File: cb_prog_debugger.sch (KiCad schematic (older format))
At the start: 49 parts, among them J1 USB_HOST, J2 Conn_01x03_Male, J3 USB_DEBUG, J4 Conn_02x03_Odd_Even, J5 ZIF16, U1 93LC56B, U2 LM1117-3.3, U3 CH341A, U4 FT232H, Y1 12 MHz, Y2 12 MHz

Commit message: Add differential net names
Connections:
- net USBDBG-: now reaches J3.2 (D-), U4.6 (DM)
- net USBDBG+: now reaches J3.3 (D+), U4.7 (DP)
- net USBHOST+: now reaches J1.3 (D+), U3.10 (UD+)
- net USBHOST-: now reaches J1.2 (D-), U3.11 (UD-)
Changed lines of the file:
@@
 Wire Wire Line
 	1400 6700 1400 6650
+Text Label 2600 2900 0    60   ~ 0
+USBHOST+
+Text Label 2600 3000 0    60   ~ 0
+USBHOST-
+Text Label 3800 5550 0    60   ~ 0
+USBDBG+
+Text Label 3800 5650 0    60   ~ 0
+USBDBG-
 $EndSCHEMATC

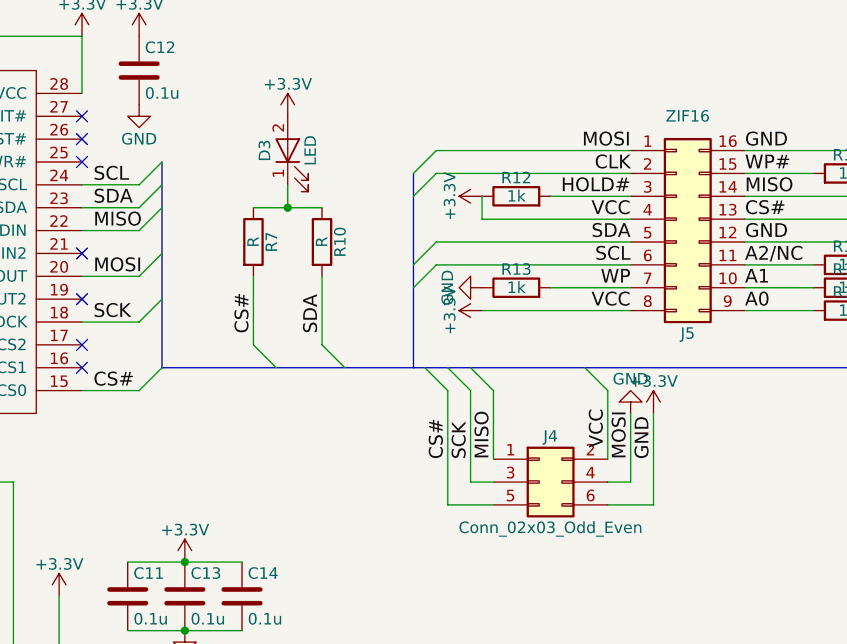
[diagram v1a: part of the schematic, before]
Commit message: Fix shorted 3.3V-GND
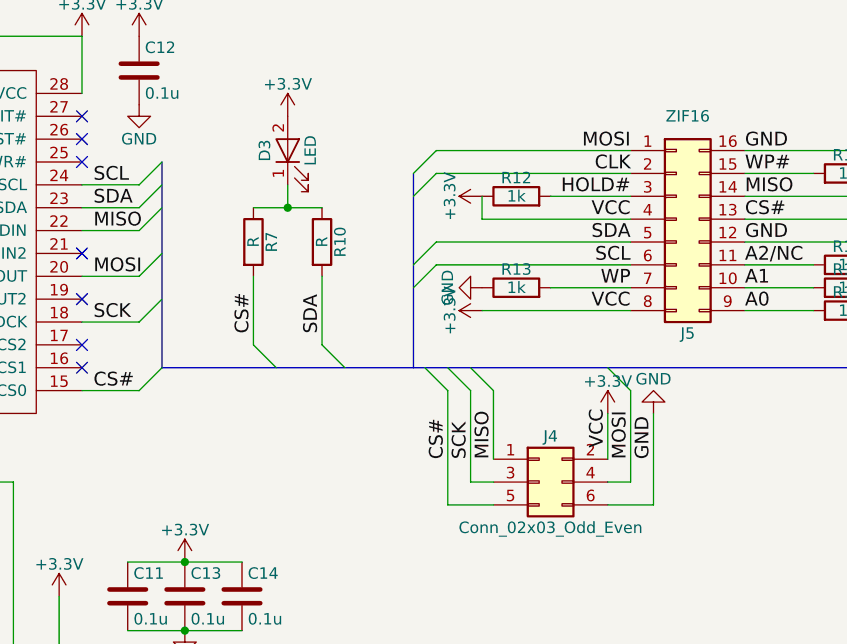
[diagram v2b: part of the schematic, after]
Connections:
- net +3V3: no longer C1.2, C10.2, C11.2, C12.2, C13.2, C14.2, C2.2, C3.2, C4.2, C5.2, C6.2, C7.2, C8.2, C9.2, D1.1 (K), D2.1 (K), J1.5 (GND), J1.6 (Shield), J2.1 (Pin_1), J3.5 (GND), J3.6 (Shield), J4.4 (Pin_4), J4.6 (Pin_6), J5.1 (Pin_1), J5.12 (Pin_12), J5.16 (Pin_16), R13.1, R15.1, R16.1, R17.1, R6.2, U1.2 (VSS), U2.1 (GND), U3.12 (GND), U3.20 (DTR#/D5/DOUT), U4.10 (GND), U4.11 (GND), U4.22 (GND), U4.23 (GND), U4.35 (GND), U4.36 (GND), U4.4 (AGND), U4.41 (AGND), U4.42 (TEST), U4.47 (GND), U4.48 (GND), U4.9 (AGND)
- new net GND: C1.2, C10.2, C11.2, C12.2, C13.2, C14.2, C2.2, C3.2, C4.2, C5.2, C6.2, C7.2, C8.2, C9.2, D1.1 (K), D2.1 (K), J1.5 (GND), J1.6 (Shield), J2.1 (Pin_1), J3.5 (GND), J3.6 (Shield), J4.6 (Pin_6), J5.12 (Pin_12), J5.16 (Pin_16), R13.1, R15.1, R16.1, R17.1, R6.2, U1.2 (VSS), U2.1 (GND), U3.12 (GND), U4.10 (GND), U4.11 (GND), U4.22 (GND), U4.23 (GND), U4.35 (GND), U4.36 (GND), U4.4 (AGND), U4.41 (AGND), U4.42 (TEST), U4.47 (GND), U4.48 (GND), U4.9 (AGND)
- new net MOSI: J4.4 (Pin_4), J5.1 (Pin_1), U3.20 (DTR#/D5/DOUT)

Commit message: Use 0805 packages
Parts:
- C1, C10, C11, C12, C13, C14, C2, C3, C4, C5, C6, C7, C8, C9: footprint Capacitors_SMD:C_1206 -> Capacitors_SMD:C_0805
- D1, D2, D3, D4, D5: footprint LEDs:LED_1206 -> LEDs:LED_0805
- L1, L2: footprint Inductors_SMD:L_1206 -> Inductors_SMD:L_0805
- R1, R10, R11, R12, R13, R14, R15, R16, R17, R2, R3, R4, R5, R6, R7, R8, R9: footprint Resistors_SMD:R_1206 -> Resistors_SMD:R_0805
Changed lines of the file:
@@
 F 0 "R1" V 2680 2000 50  0000 C CNN
 F 1 "222" V 2600 2000 50  0000 C CNN
-F 2 "Resistors_SMD:R_1206" V 2530 2000 50  0001 C CNN
+F 2 "Resistors_SMD:R_0805" V 2530 2000 50  0001 C CNN
 F 3 "" H 2600 2000 50  0001 C CNN
 	1    2600 2000
@@
 F 0 "C1" H 2825 3850 50  0000 L CNN
 F 1 "22p" H 2825 3650 50  0000 L CNN
-F 2 "Capacitors_SMD:C_1206" H 2838 3600 50  0001 C CNN
+F 2 "Capacitors_SMD:C_0805" H 2838 3600 50  0001 C CNN
 F 3 "" H 2800 3750 50  0001 C CNN
 	1    2800 3750
@@
 F 0 "C2" H 3125 3850 50  0000 L CNN
 F 1 "22p" H 3125 3650 50  0000 L CNN
-F 2 "Capacitors_SMD:C_1206" H 3138 3600 50  0001 C CNN
+F 2 "Capacitors_SMD:C_0805" H 3138 3600 50  0001 C CNN
 F 3 "" H 3100 3750 50  0001 C CNN
 	1    3100 3750
@@
 F 0 "C5" H 3625 1150 50  0000 L CNN
 F 1 "10u" H 3625 950 50  0000 L CNN
-F 2 "Capacitors_SMD:C_1206" H 3638 900 50  0001 C CNN
+F 2 "Capacitors_SMD:C_0805" H 3638 900 50  0001 C CNN
 F 3 "" H 3600 1050 50  0001 C CNN
 	1    3600 1050
@@
 F 0 "C8" H 4525 1150 50  0000 L CNN
 F 1 "10u" H 4525 950 50  0000 L CNN
-F 2 "Capacitors_SMD:C_1206" H 4538 900 50  0001 C CNN
+F 2 "Capacitors_SMD:C_0805" H 4538 900 50  0001 C CNN
 F 3 "" H 4500 1050 50  0001 C CNN
 	1    4500 1050
@@
 F 0 "R3" V 2980 850 50  0000 C CNN
 F 1 "R" V 2900 850 50  0000 C CNN
-F 2 "Resistors_SMD:R_1206" V 2830 850 50  0001 C CNN
+F 2 "Resistors_SMD:R_0805" V 2830 850 50  0001 C CNN
 F 3 "" H 2900 850 50  0001 C CNN
 	1    2900 850
@@
 F 0 "D2" H 2900 1250 50  0000 C CNN
 F 1 "PWRLED" H 2900 1050 50  0000 C CNN
-F 2 "LEDs:LED_1206" H 2900 1150 50  0001 C CNN
+F 2 "LEDs:LED_0805" H 2900 1150 50  0001 C CNN
 F 3 "" H 2900 1150 50  0001 C CNN
 	1    2900 1150
@@
 F 0 "C12" H 5775 2000 50  0000 L CNN
 F 1 "0.1u" H 5775 1800 50  0000 L CNN
-F 2 "Capacitors_SMD:C_1206" H 5788 1750 50  0001 C CNN
+F 2 "Capacitors_SMD:C_0805" H 5788 1750 50  0001 C CNN
 F 3 "" H 5750 1900 50  0001 C CNN
 	1    5750 1900
@@
 F 0 "R12" V 7480 2450 50  0000 C CNN
 F 1 "1k" V 7400 2450 50  0000 C CNN
-F 2 "Resistors_SMD:R_1206" V 7330 2450 50  0001 C CNN
+F 2 "Resistors_SMD:R_0805" V 7330 2450 50  0001 C CNN
 F 3 "" H 7400 2450 50  0001 C CNN
 	1    7400 2450
@@
 F 0 "R14" V 8930 2350 50  0000 C CNN
 F 1 "1k" V 8850 2350 50  0000 C CNN
-F 2 "Resistors_SMD:R_1206" V 8780 2350 50  0001 C CNN
+F 2 "Resistors_SMD:R_0805" V 8780 2350 50  0001 C CNN
 F 3 "" H 8850 2350 50  0001 C CNN
 	1    8850 2350
@@
 F 0 "R15" V 8930 2750 50  0000 C CNN
 F 1 "1k" V 8850 2750 50  0000 C CNN
-F 2 "Resistors_SMD:R_1206" V 8780 2750 50  0001 C CNN
+F 2 "Resistors_SMD:R_0805" V 8780 2750 50  0001 C CNN
 F 3 "" H 8850 2750 50  0001 C CNN
 	1    8850 2750
@@
 F 0 "R16" V 8930 2850 50  0000 C CNN
 F 1 "1k" V 8850 2850 50  0000 C CNN
-F 2 "Resistors_SMD:R_1206" V 8780 2850 50  0001 C CNN
+F 2 "Resistors_SMD:R_0805" V 8780 2850 50  0001 C CNN
 F 3 "" H 8850 2850 50  0001 C CNN
 	1    8850 2850
@@
 F 0 "R17" V 8930 2950 50  0000 C CNN
 F 1 "1k" V 8850 2950 50  0000 C CNN
-F 2 "Resistors_SMD:R_1206" V 8780 2950 50  0001 C CNN
+F 2 "Resistors_SMD:R_0805" V 8780 2950 50  0001 C CNN
 F 3 "" H 8850 2950 50  0001 C CNN
 	1    8850 2950
@@
 F 0 "R13" V 7480 2850 50  0000 C CNN
 F 1 "1k" V 7400 2850 50  0000 C CNN
-F 2 "Resistors_SMD:R_1206" V 7330 2850 50  0001 C CNN
+F 2 "Resistors_SMD:R_0805" V 7330 2850 50  0001 C CNN
 F 3 "" H 7400 2850 50  0001 C CNN
 	1    7400 2850
@@
 F 0 "R7" V 6330 2650 50  0000 C CNN
 F 1 "R" V 6250 2650 50  0000 C CNN
-F 2 "Resistors_SMD:R_1206" V 6180 2650 50  0001 C CNN
+F 2 "Resistors_SMD:R_0805" V 6180 2650 50  0001 C CNN
 F 3 "" H 6250 2650 50  0001 C CNN
 	1    6250 2650
@@
 F 0 "D3" H 6400 2350 50  0000 C CNN
 F 1 "LED" H 6400 2150 50  0000 C CNN
-F 2 "LEDs:LED_1206" H 6400 2250 50  0001 C CNN
+F 2 "LEDs:LED_0805" H 6400 2250 50  0001 C CNN
 F 3 "" H 6400 2250 50  0001 C CNN
 	1    6400 2250
@@
 F 0 "R10" V 6630 2650 50  0000 C CNN
 F 1 "R" V 6550 2650 50  0000 C CNN
-F 2 "Resistors_SMD:R_1206" V 6480 2650 50  0001 C CNN
+F 2 "Resistors_SMD:R_0805" V 6480 2650 50  0001 C CNN
 F 3 "" H 6550 2650 50  0001 C CNN
 	1    6550 2650
@@
 F 0 "C10" H 4875 4450 50  0000 L CNN
 F 1 "10u" H 4875 4250 50  0000 L CNN
-F 2 "Capacitors_SMD:C_1206" H 4888 4200 50  0001 C CNN
+F 2 "Capacitors_SMD:C_0805" H 4888 4200 50  0001 C CNN
 F 3 "" H 4850 4350 50  0001 C CNN
 	1    4850 4350
@@
 F 0 "C9" H 4875 3950 50  0000 L CNN
 F 1 "10u" H 4875 3750 50  0000 L CNN
-F 2 "Capacitors_SMD:C_1206" H 4888 3700 50  0001 C CNN
+F 2 "Capacitors_SMD:C_0805" H 4888 3700 50  0001 C CNN
 F 3 "" H 4850 3850 50  0001 C CNN
 	1    4850 3850
@@
 F 0 "C4" H 3525 5050 50  0000 L CNN
 F 1 "0.1u" H 3525 4850 50  0000 L CNN
-F 2 "Capacitors_SMD:C_1206" H 3538 4800 50  0001 C CNN
+F 2 "Capacitors_SMD:C_0805" H 3538 4800 50  0001 C CNN
 F 3 "" H 3500 4950 50  0001 C CNN
 	1    3500 4950
@@
 F 0 "C3" H 3525 4850 50  0000 L CNN
 F 1 "0.1u" H 3525 4650 50  0000 L CNN
-F 2 "Capacitors_SMD:C_1206" H 3538 4600 50  0001 C CNN
+F 2 "Capacitors_SMD:C_0805" H 3538 4600 50  0001 C CNN
 F 3 "" H 3500 4750 50  0001 C CNN
 	1    3500 4750
@@
 F 0 "L1" H 4500 3800 50  0000 C CNN
 F 1 "INDUCTOR" H 4500 3650 50  0000 C CNN
-F 2 "Inductors_SMD:L_1206" H 4500 3700 50  0001 C CNN
+F 2 "Inductors_SMD:L_0805" H 4500 3700 50  0001 C CNN
 F 3 "" H 4500 3700 50  0001 C CNN
 	1    4500 3700
@@
 F 0 "L2" H 4500 4300 50  0000 C CNN
 F 1 "INDUCTOR" H 4500 4150 50  0000 C CNN
-F 2 "Inductors_SMD:L_1206" H 4500 4200 50  0001 C CNN
+F 2 "Inductors_SMD:L_0805" H 4500 4200 50  0001 C CNN
 F 3 "" H 4500 4200 50  0001 C CNN
 	1    4500 4200
@@
 F 0 "C6" H 3725 7200 50  0000 L CNN
 F 1 "22p" H 3725 7000 50  0000 L CNN
-F 2 "Capacitors_SMD:C_1206" H 3738 6950 50  0001 C CNN
+F 2 "Capacitors_SMD:C_0805" H 3738 6950 50  0001 C CNN
 F 3 "" H 3700 7100 50  0001 C CNN
 	1    3700 7100
@@
 F 0 "C7" H 4025 7200 50  0000 L CNN
 F 1 "22p" H 4025 7000 50  0000 L CNN
-F 2 "Capacitors_SMD:C_1206" H 4038 6950 50  0001 C CNN
+F 2 "Capacitors_SMD:C_0805" H 4038 6950 50  0001 C CNN
 F 3 "" H 4000 7100 50  0001 C CNN
 	1    4000 7100
@@
 F 0 "R6" V 4330 5950 50  0000 C CNN
 F 1 "12k" V 4250 5950 50  0000 C CNN
-F 2 "Resistors_SMD:R_1206" V 4180 5950 50  0001 C CNN
+F 2 "Resistors_SMD:R_0805" V 4180 5950 50  0001 C CNN
 F 3 "" H 4250 5950 50  0001 C CNN
 F 4 "1%" V 4150 5950 60  0000 C CNN "Precision"
@@
 F 0 "R5" V 4330 5750 50  0000 C CNN
 F 1 "12k" V 4250 5750 50  0000 C CNN
-F 2 "Resistors_SMD:R_1206" V 4180 5750 50  0001 C CNN
+F 2 "Resistors_SMD:R_0805" V 4180 5750 50  0001 C CNN
 F 3 "" H 4250 5750 50  0001 C CNN
 	1    4250 5750
@@
 F 0 "R4" V 1480 6500 50  0000 C CNN
 F 1 "2.2k" V 1400 6500 50  0000 C CNN
-F 2 "Resistors_SMD:R_1206" V 1330 6500 50  0001 C CNN
+F 2 "Resistors_SMD:R_0805" V 1330 6500 50  0001 C CNN
 F 3 "" H 1400 6500 50  0001 C CNN
 	1    1400 6500
@@
 F 0 "R9" V 6580 5550 50  0000 C CNN
 F 1 "R" V 6500 5550 50  0000 C CNN
-F 2 "Resistors_SMD:R_1206" V 6430 5550 50  0001 C CNN
+F 2 "Resistors_SMD:R_0805" V 6430 5550 50  0001 C CNN
 F 3 "" H 6500 5550 50  0001 C CNN
 	1    6500 5550
@@
 F 0 "D4" H 6500 5950 50  0000 C CNN
 F 1 "RXLED" H 6500 5750 50  0000 C CNN
-F 2 "LEDs:LED_1206" H 6500 5850 50  0001 C CNN
+F 2 "LEDs:LED_0805" H 6500 5850 50  0001 C CNN
 F 3 "" H 6500 5850 50  0001 C CNN
 	1    6500 5850
@@
 F 0 "R11" V 6880 5550 50  0000 C CNN
 F 1 "R" V 6800 5550 50  0000 C CNN
-F 2 "Resistors_SMD:R_1206" V 6730 5550 50  0001 C CNN
+F 2 "Resistors_SMD:R_0805" V 6730 5550 50  0001 C CNN
 F 3 "" H 6800 5550 50  0001 C CNN
 	1    6800 5550
@@
 F 0 "D5" H 6800 5950 50  0000 C CNN
 F 1 "TXLED" H 6800 5750 50  0000 C CNN
-F 2 "LEDs:LED_1206" H 6800 5850 50  0001 C CNN
+F 2 "LEDs:LED_0805" H 6800 5850 50  0001 C CNN
 F 3 "" H 6800 5850 50  0001 C CNN
 	1    6800 5850
@@
 F 0 "R8" V 6430 6450 50  0000 C CNN
 F 1 "12k" V 6350 6450 50  0000 C CNN
-F 2 "Resistors_SMD:R_1206" V 6280 6450 50  0001 C CNN
+F 2 "Resistors_SMD:R_0805" V 6280 6450 50  0001 C CNN
 F 3 "" H 6350 6450 50  0001 C CNN
 	1    6350 6450
@@
 F 0 "C13" H 5975 4300 50  0000 L CNN
 F 1 "0.1u" H 5975 4100 50  0000 L CNN
-F 2 "Capacitors_SMD:C_1206" H 5988 4050 50  0001 C CNN
+F 2 "Capacitors_SMD:C_0805" H 5988 4050 50  0001 C CNN
 F 3 "" H 5950 4200 50  0001 C CNN
 	1    5950 4200
@@
 F 0 "C14" H 6225 4300 50  0000 L CNN
 F 1 "0.1u" H 6225 4100 50  0000 L CNN
-F 2 "Capacitors_SMD:C_1206" H 6238 4050 50  0001 C CNN
+F 2 "Capacitors_SMD:C_0805" H 6238 4050 50  0001 C CNN
 F 3 "" H 6200 4200 50  0001 C CNN
 	1    6200 4200
@@
 F 0 "C11" H 5725 4300 50  0000 L CNN
 F 1 "0.1u" H 5725 4100 50  0000 L CNN
-F 2 "Capacitors_SMD:C_1206" H 5738 4050 50  0001 C CNN
+F 2 "Capacitors_SMD:C_0805" H 5738 4050 50  0001 C CNN
 F 3 "" H 5700 4200 50  0001 C CNN
 	1    5700 4200
@@
 F 0 "R2" V 2880 5300 50  0000 C CNN
 F 1 "R" V 2800 5300 50  0000 C CNN
-F 2 "Resistors_SMD:R_1206" V 2730 5300 50  0001 C CNN
+F 2 "Resistors_SMD:R_0805" V 2730 5300 50  0001 C CNN
 F 3 "" H 2800 5300 50  0001 C CNN
 	1    2800 5300
@@
 F 0 "D1" H 2800 5700 50  0000 C CNN
 F 1 "DBGLED" H 2800 5500 50  0000 C CNN
-F 2 "LEDs:LED_1206" H 2800 5600 50  0001 C CNN
+F 2 "LEDs:LED_0805" H 2800 5600 50  0001 C CNN
 F 3 "" H 2800 5600 50  0001 C CNN
 	1    2800 5600
